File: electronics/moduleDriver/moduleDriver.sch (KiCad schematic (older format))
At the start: 65 parts, among them J1 Power In, J10 12V SENSE, J2 UART, J3 SENSOR, J4 5V, J5 GND, J8 RS485, J9 RS485, U1 Mega2560Shield, U10 ULN2003A_E, U11 INA219 Breakout Wide (blue), U12 ULN2003A_D, U13 ULN2003A_C, U14 ULN2003A_B, U15 ULN2003A_A, U17 RS485Module, U2 SSD1306_I2C, U3 ULN2003A_L, U31 INA219 Breakout Narrow (purpl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, U32 SP485, U33 INA219BxD, U4 ULN2003A_K, U5 ULN2003A_J, U6 ULN2003A_I, U7 ULN2003A_H, U8 ULN2003A_G, U9 ULN2003A_F

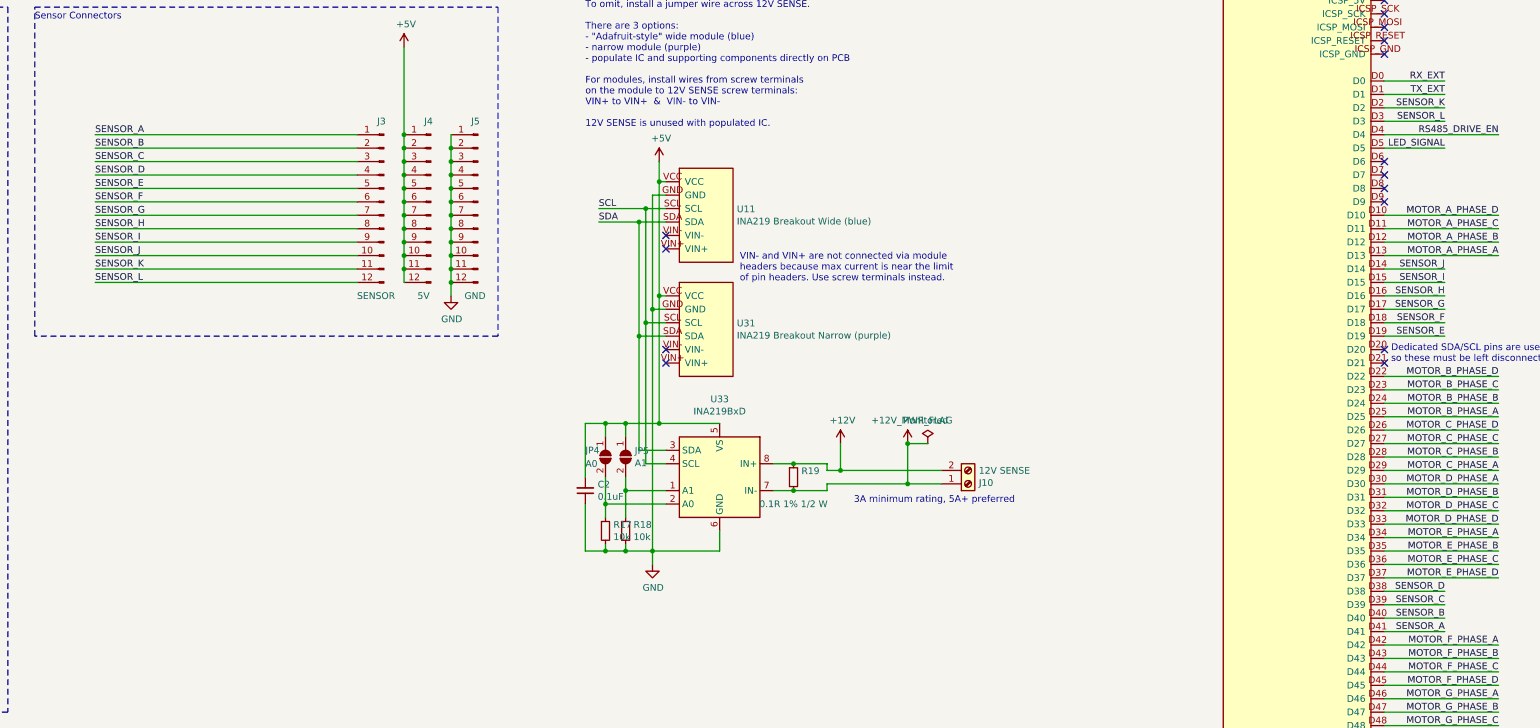
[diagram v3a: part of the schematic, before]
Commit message: Silkscreen cleanup
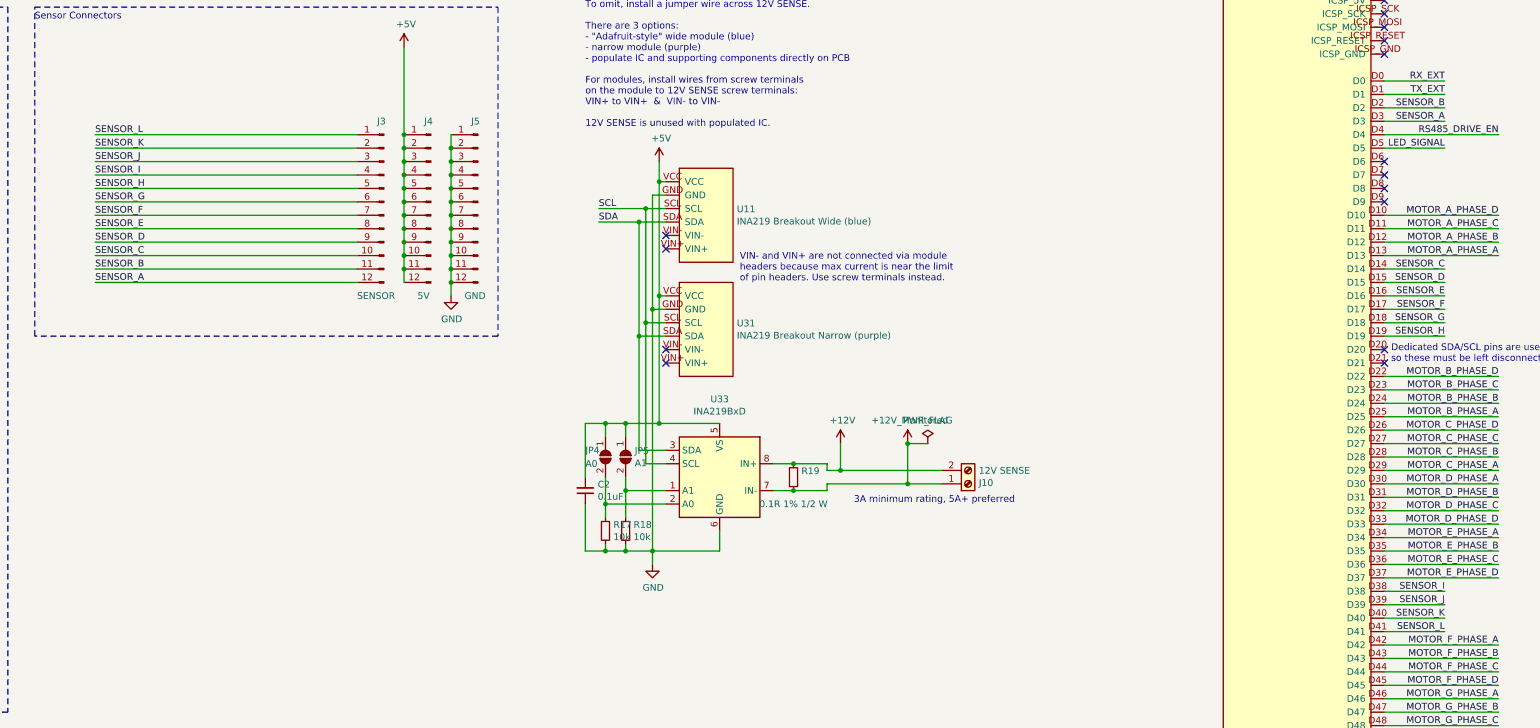
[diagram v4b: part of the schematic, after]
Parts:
- U1: footprint Mega2560Shield:Mega2560Shield -> Mega2560Shield:Mega2560Shield_Modified
- U10, U12, U13, U14, U15, U3, U4, U5, U6, U7, U8, U9: footprint ULN2003AModule:ULN2003AModule_No_EN -> ULN2003AModule:ULN2003AModule_No_EN_No_FSilk
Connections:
- net SENSOR_A: now also J3.12 (Pin_12), U1.D3; no longer J3.1 (Pin_1), U1.D41
- net SENSOR_B: now also J3.11 (Pin_11), U1.D2; no longer J3.2 (Pin_2), U1.D40
- net SENSOR_C: now also J3.10 (Pin_10), U1.D14; no longer J3.3 (Pin_3), U1.D39
- net SENSOR_D: now also J3.9 (Pin_9), U1.D15; no longer J3.4 (Pin_4), U1.D38
- net SENSOR_E: now also J3.8 (Pin_8), U1.D16; no longer J3.5 (Pin_5), U1.D19
- net SENSOR_F: now also J3.7 (Pin_7), U1.D17; no longer J3.6 (Pin_6), U1.D18
- net SENSOR_G: now also J3.6 (Pin_6), U1.D18; no longer J3.7 (Pin_7), U1.D17
- net SENSOR_H: now also J3.5 (Pin_5), U1.D19; no longer J3.8 (Pin_8), U1.D16
- net SENSOR_I: now also J3.4 (Pin_4), U1.D38; no longer J3.9 (Pin_9), U1.D15
- net SENSOR_J: now also J3.3 (Pin_3), U1.D39; no longer J3.10 (Pin_10), U1.D14
- net SENSOR_K: now also J3.2 (Pin_2), U1.D40; no longer J3.11 (Pin_11), U1.D2
- net SENSOR_L: now also J3.1 (Pin_1), U1.D41; no longer J3.12 (Pin_12), U1.D3
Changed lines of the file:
@@
 F 0 "U3" H 2100 3000 50  0000 C CNN
 F 1 "ULN2003A_L" H 2350 2900 50  0000 C CNN
-F 2 "ULN2003AModule:ULN2003AModule_No_EN" H 1800 2600 50  0001 C CNN
+F 2 "ULN2003AModule:ULN2003AModule_No_EN_No_FSilk" H 1800 2600 50  0001 C CNN
 F 3 "" H 1800 2600 50  0001 C CNN
 	1    1600 2850
@@
 F 0 "U4" H 4150 3000 50  0000 C CNN
 F 1 "ULN2003A_K" H 4400 2900 50  0000 C CNN
-F 2 "ULN2003AModule:ULN2003AModule_No_EN" H 3850 2600 50  0001 C CNN
+F 2 "ULN2003AModule:ULN2003AModule_No_EN_No_FSilk" H 3850 2600 50  0001 C CNN
 F 3 "" H 3850 2600 50  0001 C CNN
 	1    3650 2850
@@
 F 0 "U5" H 6200 3000 50  0000 C CNN
 F 1 "ULN2003A_J" H 6450 2900 50  0000 C CNN
-F 2 "ULN2003AModule:ULN2003AModule_No_EN" H 5900 2600 50  0001 C CNN
+F 2 "ULN2003AModule:ULN2003AModule_No_EN_No_FSilk" H 5900 2600 50  0001 C CNN
 F 3 "" H 5900 2600 50  0001 C CNN
 	1    5700 2850
@@
 F 0 "U6" H 8250 3000 50  0000 C CNN
 F 1 "ULN2003A_I" H 8500 2900 50  0000 C CNN
-F 2 "ULN2003AModule:ULN2003AModule_No_EN" H 7950 2600 50  0001 C CNN
+F 2 "ULN2003AModule:ULN2003AModule_No_EN_No_FSilk" H 7950 2600 50  0001 C CNN
 F 3 "" H 7950 2600 50  0001 C CNN
 	1    7750 2850
@@
 F 0 "U7" H 2100 4700 50  0000 C CNN
 F 1 "ULN2003A_H" H 2350 4600 50  0000 C CNN
-F 2 "ULN2003AModule:ULN2003AModule_No_EN" H 1800 4300 50  0001 C CNN
+F 2 "ULN2003AModule:ULN2003AModule_No_EN_No_FSilk" H 1800 4300 50  0001 C CNN
 F 3 "" H 1800 4300 50  0001 C CNN
 	1    1600 4550
@@
 F 0 "U8" H 4150 4700 50  0000 C CNN
 F 1 "ULN2003A_G" H 4400 4600 50  0000 C CNN
-F 2 "ULN2003AModule:ULN2003AModule_No_EN" H 3850 4300 50  0001 C CNN
+F 2 "ULN2003AModule:ULN2003AModule_No_EN_No_FSilk" H 3850 4300 50  0001 C CNN
 F 3 "" H 3850 4300 50  0001 C CNN
 	1    3650 4550
@@
 F 0 "U9" H 6200 4700 50  0000 C CNN
 F 1 "ULN2003A_F" H 6450 4600 50  0000 C CNN
-F 2 "ULN2003AModule:ULN2003AModule_No_EN" H 5900 4300 50  0001 C CNN
+F 2 "ULN2003AModule:ULN2003AModule_No_EN_No_FSilk" H 5900 4300 50  0001 C CNN
 F 3 "" H 5900 4300 50  0001 C CNN
 	1    5700 4550
@@
 F 0 "U10" H 8250 4700 50  0000 C CNN
 F 1 "ULN2003A_E" H 8500 4600 50  0000 C CNN
-F 2 "ULN2003AModule:ULN2003AModule_No_EN" H 7950 4300 50  0001 C CNN
+F 2 "ULN2003AModule:ULN2003AModule_No_EN_No_FSilk" H 7950 4300 50  0001 C CNN
 F 3 "" H 7950 4300 50  0001 C CNN
 	1    7750 4550
@@
 F 0 "U12" H 2100 6400 50  0000 C CNN
 F 1 "ULN2003A_D" H 2350 6300 50  0000 C CNN
-F 2 "ULN2003AModule:ULN2003AModule_No_EN" H 1800 6000 50  0001 C CNN
+F 2 "ULN2003AModule:ULN2003AModule_No_EN_No_FSilk" H 1800 6000 50  0001 C CNN
 F 3 "" H 1800 6000 50  0001 C CNN
 	1    1600 6250
@@
 F 0 "U13" H 4150 6400 50  0000 C CNN
 F 1 "ULN2003A_C" H 4400 6300 50  0000 C CNN
-F 2 "ULN2003AModule:ULN2003AModule_No_EN" H 3850 6000 50  0001 C CNN
+F 2 "ULN2003AModule:ULN2003AModule_No_EN_No_FSilk" H 3850 6000 50  0001 C CNN
 F 3 "" H 3850 6000 50  0001 C CNN
 	1    3650 6250
@@
 F 0 "U14" H 6200 6400 50  0000 C CNN
 F 1 "ULN2003A_B" H 6450 6300 50  0000 C CNN
-F 2 "ULN2003AModule:ULN2003AModule_No_EN" H 5900 6000 50  0001 C CNN
+F 2 "ULN2003AModule:ULN2003AModule_No_EN_No_FSilk" H 5900 6000 50  0001 C CNN
 F 3 "" H 5900 6000 50  0001 C CNN
 	1    5700 6250
@@
 F 0 "U15" H 8250 6400 50  0000 C CNN
 F 1 "ULN2003A_A" H 8500 6300 50  0000 C CNN
-F 2 "ULN2003AModule:ULN2003AModule_No_EN" H 7950 6000 50  0001 C CNN
+F 2 "ULN2003AModule:ULN2003AModule_No_EN_No_FSilk" H 7950 6000 50  0001 C CNN
 F 3 "" H 7950 6000 50  0001 C CNN
 	1    7750 6250
@@
 F 0 "U1" H 18725 1065 50  0000 C CNN
 F 1 "Mega2560Shield" H 18725 974 50  0000 C CNN
-F 2 "Mega2560Shield:Mega2560Shield" H 17150 1000 50  0001 C CNN
+F 2 "Mega2560Shield:Mega2560Shield_Modified" H 17150 1000 50  0001 C CNN
 F 3 "" H 17150 1000 50  0001 C CNN
 	1    18050 900
@@
 Wire Wire Line
 	1350 1350 800  1350
+Text Label 19700 3100 2    50   ~ 0
+SENSOR_A
+Wire Wire Line
+	19700 6900 19250 6900
+Text Label 19700 3000 2    50   ~ 0
+SENSOR_B
+Wire Wire Line
+	19700 6800 19250 6800
+Text Label 19700 4200 2    50   ~ 0
+SENSOR_C
+Wire Wire Line
+	19700 6700 19250 6700
+Text Label 19700 4300 2    50   ~ 0
+SENSOR_D
+Wire Wire Line
+	19700 6600 19250 6600
+Text Label 19700 4400 2    50   ~ 0
+SENSOR_E
+Wire Wire Line
+	19700 4700 19250 4700
+Text Label 19700 4500 2    50   ~ 0
+SENSOR_F
+Wire Wire Line
+	19700 4600 19250 4600
+Text Label 19700 4600 2    50   ~ 0
+SENSOR_G
+Wire Wire Line
+	19700 4500 19250 4500
+Text Label 19700 4700 2    50   ~ 0
+SENSOR_H
+Wire Wire Line
+	19700 4400 19250 4400
+Text Label 19700 6600 2    50   ~ 0
+SENSOR_I
+Wire Wire Line
+	19700 4300 19250 4300
+Text Label 19700 6700 2    50   ~ 0
+SENSOR_J
+Wire Wire Line
+	19700 4200 19250 4200
 Text Label 19700 6900 2    50   ~ 0
-SENSOR_A
-Wire Wire Line
-	19700 6900 19250 6900
+SENSOR_L
+Wire Wire Line
+	19700 3100 19250 3100
 Text Label 19700 6800 2    50   ~ 0
-SENSOR_B
-Wire Wire Line
-	19700 6800 19250 6800
-Text Label 19700 6700 2    50   ~ 0
-SENSOR_C
-Wire Wire Line
-	19700 6700 19250 6700
-Text Label 19700 6600 2    50   ~ 0
-SENSOR_D
-Wire Wire Line
-	19700 6600 19250 6600
-Text Label 19700 4700 2    50   ~ 0
-SENSOR_E
-Wire Wire Line
-	19700 4700 19250 4700
-Text Label 19700 4600 2    50   ~ 0
-SENSOR_F
-Wire Wire Line
-	19700 4600 19250 4600
-Text Label 19700 4500 2    50   ~ 0
-SENSOR_G
-Wire Wire Line
-	19700 4500 19250 4500
-Text Label 19700 4400 2    50   ~ 0
-SENSOR_H
-Wire Wire Line
-	19700 4400 19250 4400
-Text Label 19700 4300 2    50   ~ 0
-SENSOR_I
-Wire Wire Line
-	19700 4300 19250 4300
-Text Label 19700 4200 2    50   ~ 0
-SENSOR_J
-Wire Wire Line
-	19700 4200 19250 4200
-Text Label 19700 3100 2    50   ~ 0
-SENSOR_L
-Wire Wire Line
-	19700 3100 19250 3100
-Text Label 19700 3000 2    50   ~ 0
 SENSOR_K
 Wire Wire Line
@@
 	-1   0    0    -1
 $EndComp
+Text Label 9650 4300 0    50   ~ 0
+SENSOR_A
+Text Label 9650 4200 0    50   ~ 0
+SENSOR_B
+Text Label 9650 4100 0    50   ~ 0
+SENSOR_C
+Text Label 9650 4000 0    50   ~ 0
+SENSOR_D
+Text Label 9650 3900 0    50   ~ 0
+SENSOR_E
+Text Label 9650 3800 0    50   ~ 0
+SENSOR_F
+Text Label 9650 3700 0    50   ~ 0
+SENSOR_G
+Text Label 9650 3600 0    50   ~ 0
+SENSOR_H
+Text Label 9650 3500 0    50   ~ 0
+SENSOR_I
+Text Label 9650 3400 0    50   ~ 0
+SENSOR_J
+Text Label 9650 3300 0    50   ~ 0
+SENSOR_K
 Text Label 9650 3200 0    50   ~ 0
-SENSOR_A
-Text Label 9650 3300 0    50   ~ 0
-SENSOR_B
-Text Label 9650 3400 0    50   ~ 0
-SENSOR_C
-Text Label 9650 3500 0    50   ~ 0
-SENSOR_D
-Text Label 9650 3600 0    50   ~ 0
-SENSOR_E
-Text Label 9650 3700 0    50   ~ 0
-SENSOR_F
-Text Label 9650 3800 0    50   ~ 0
-SENSOR_G
-Text Label 9650 3900 0    50   ~ 0
-SENSOR_H
-Text Label 9650 4000 0    50   ~ 0
-SENSOR_I
-Text Label 9650 4100 0    50   ~ 0
-SENSOR_J
-Text Label 9650 4200 0    50   ~ 0
-SENSOR_K
-Text Label 9650 4300 0    50   ~ 0
 SENSOR_L
 $Comp

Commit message: Change to plated holes
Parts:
- H1, H2, H3, H4: footprint MountingHole:MountingHole_4.3mm_M4_ISO7380 -> MountingHole:MountingHole_4.3mm_M4_ISO7380_Pad
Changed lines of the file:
@@
 F 0 "H1" H 8700 1046 50  0000 L CNN
 F 1 "MountingHole" H 8700 955 50  0000 L CNN
-F 2 "MountingHole:MountingHole_4.3mm_M4_ISO7380" H 8600 1000 50  0001 C CNN
+F 2 "MountingHole:MountingHole_4.3mm_M4_ISO7380_Pad" H 8600 1000 50  0001 C CNN
 F 3 "~" H 8600 1000 50  0001 C CNN
 	1    8600 1000
@@
 F 0 "H2" H 8950 1046 50  0000 L CNN
 F 1 "MountingHole" H 8950 955 50  0000 L CNN
-F 2 "MountingHole:MountingHole_4.3mm_M4_ISO7380" H 8850 1000 50  0001 C CNN
+F 2 "MountingHole:MountingHole_4.3mm_M4_ISO7380_Pad" H 8850 1000 50  0001 C CNN
 F 3 "~" H 8850 1000 50  0001 C CNN
 	1    8850 1000
@@
 F 0 "H3" H 9200 1046 50  0000 L CNN
 F 1 "MountingHole" H 9200 955 50  0000 L CNN
-F 2 "MountingHole:MountingHole_4.3mm_M4_ISO7380" H 9100 1000 50  0001 C CNN
+F 2 "MountingHole:MountingHole_4.3mm_M4_ISO7380_Pad" H 9100 1000 50  0001 C CNN
 F 3 "~" H 9100 1000 50  0001 C CNN
 	1    9100 1000
@@
 F 0 "H4" H 9450 1046 50  0000 L CNN
 F 1 "MountingHole" H 9450 955 50  0000 L CNN
-F 2 "MountingHole:MountingHole_4.3mm_M4_ISO7380" H 9350 1000 50  0001 C CNN
+F 2 "MountingHole:MountingHole_4.3mm_M4_ISO7380_Pad" H 9350 1000 50  0001 C CNN
 F 3 "~" H 9350 1000 50  0001 C CNN
 	1    9350 1000

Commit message: Mega tweaks for alpha PCB order
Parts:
- H1, H2, H3, H4: symbol Mechanical:MountingHole -> Mechanical:MountingHole_Pad
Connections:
- no-connect marks 24 -> 28
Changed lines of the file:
@@
 	14850 5850 14700 5850
 $Comp
-L Mechanical:MountingHole H1
+L Mechanical:MountingHole_Pad H1
 U 1 1 61902623
 P 8600 1000
@@
 $EndComp
 $Comp
-L Mechanical:MountingHole H2
+L Mechanical:MountingHole_Pad H2
 U 1 1 619139E1
 P 8850 1000
@@
 $EndComp
 $Comp
-L Mechanical:MountingHole H3
+L Mechanical:MountingHole_Pad H3
 U 1 1 61913E82
 P 9100 1000
@@
 $EndComp
 $Comp
-L Mechanical:MountingHole H4
+L Mechanical:MountingHole_Pad H4
 U 1 1 61914268
 P 9350 1000
@@
 Text Notes 19300 4900 0    50   ~ 0
 Dedicated SDA/SCL pins are used,\nso these must be left disconnected.
+NoConn ~ 8600 1100
+NoConn ~ 8850 1100
+NoConn ~ 9100 1100
+NoConn ~ 9350 1100
 $EndSCHEMATC
